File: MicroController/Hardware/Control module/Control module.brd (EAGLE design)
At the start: 100 x 60 mm, 54 parts, among them J1 1X2-3.5MM, J2 RJ45-TRAFO, J3 RJ45-TRAFO, J4 RJ45-TRAFO, Q1 BSS138, Q2 BSS138, Q3 BSS138, Q4 BSS138, Q5 BSS138, Q6 BSS138, Q7 BSS138, Q8 BSS138, U1 CD74HC4067SM96, U3 TLV1117-33CDCY

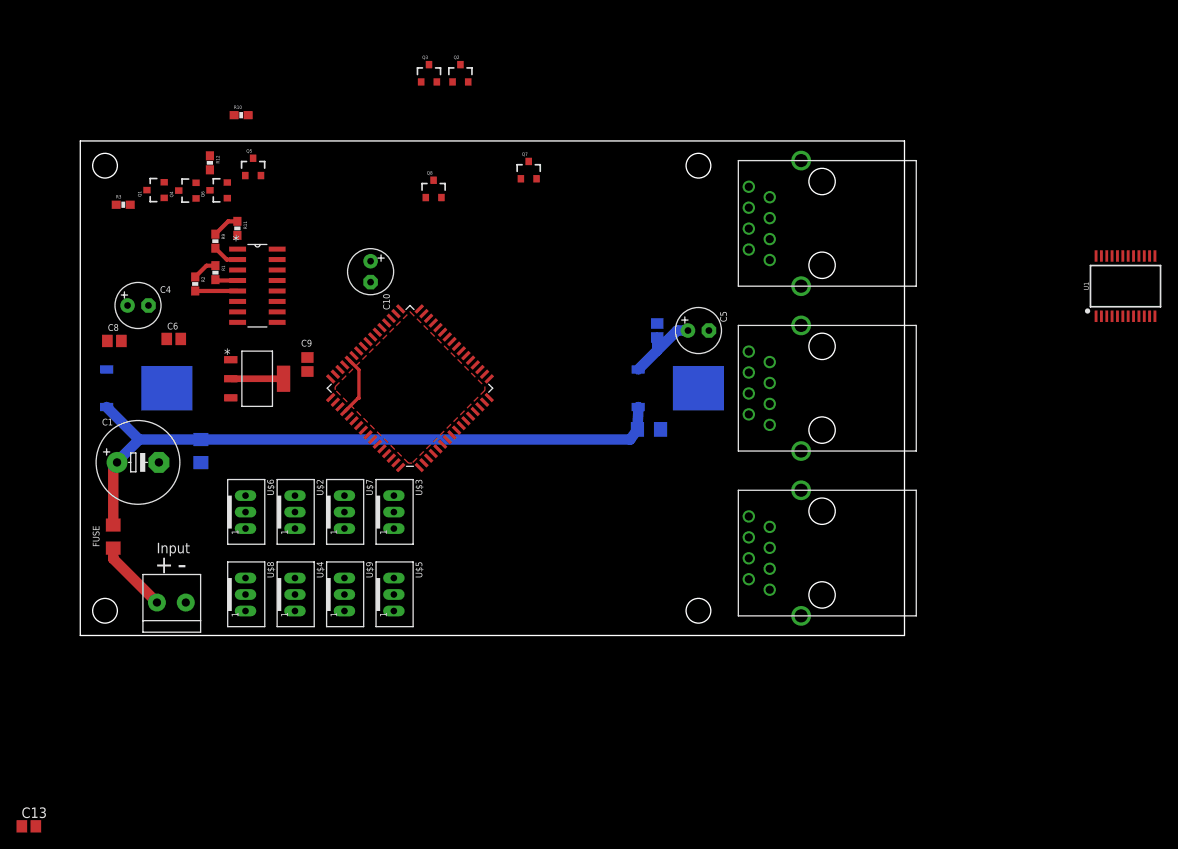
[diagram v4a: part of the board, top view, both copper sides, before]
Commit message: Connected several components, added RX TX connector
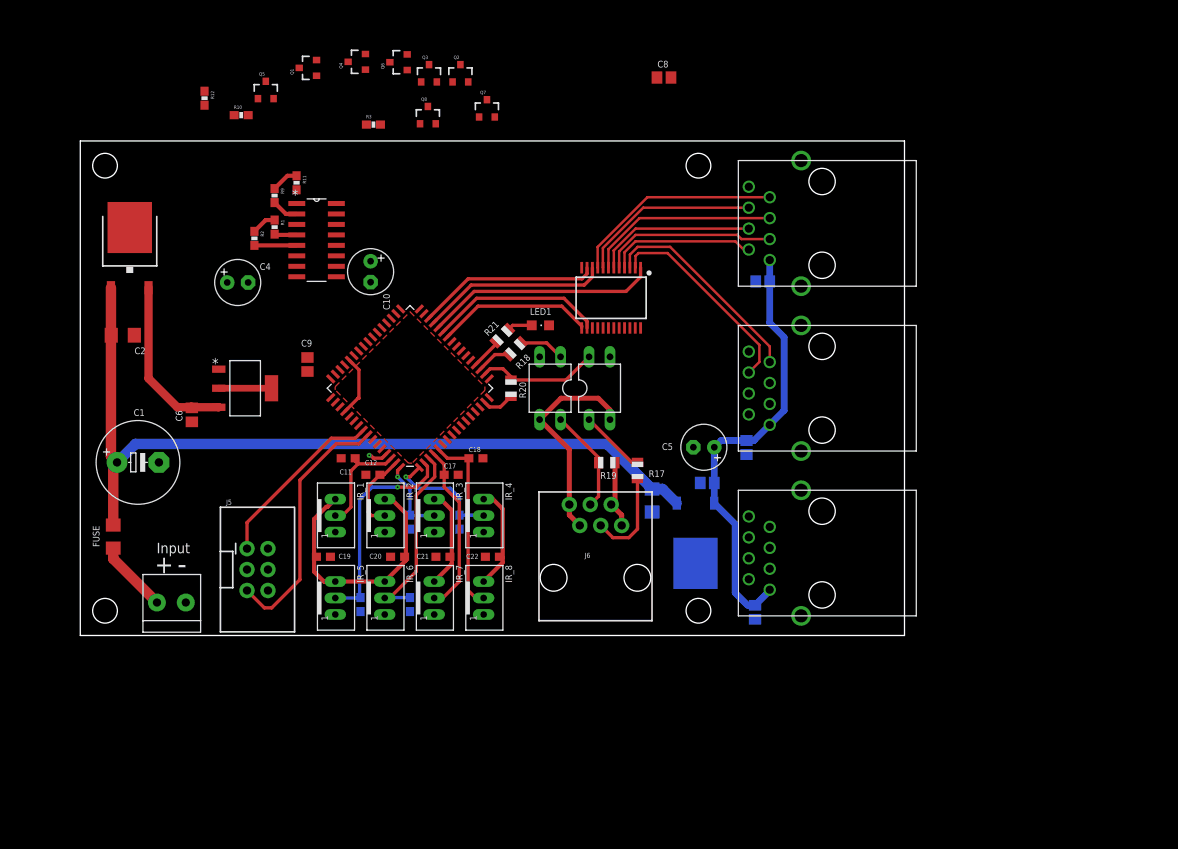
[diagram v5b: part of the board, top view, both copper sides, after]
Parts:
- removed U$2, U$3, U$4, U$5, U$6, U$7, U$8, U$9: JST-PH_3-PIN_HEADER, SRG:JST_B3B-PH_HEADER
- added C11, C12, C14, C15, C16, C17, C18, C19, C20, C21, C22: (no value), adafruit:C0603
- added C23, C24, C25: (no value), adafruit:C0805
- added IR_1, IR_2, IR_3, IR_4, IR_5, IR_6, IR_7, IR_8: JST-PH_3-PIN_HEADER, SRG:JST_B3B-PH_HEADER
- added J5: (no value), SparkFun-Connectors:2X3-SHROUDED
- added J6: RJ11, SparkFun-Connectors:RJ11-6
- added LED1: (no value), led:CHIPLED_0805
- added OC1, OC2: (no value), optocoupler:DIL04
- added R17, R18, R19, R20, R21: 10K, adafruit:R0805
- C13: device adafruit:C0805 -> adafruit:C0603
- moved C8 73.9 mm to (70.8, 67.7)
- moved U1 62.4 mm to (64.4, 41.0), turned to 180 degrees
- moved C13 48.4 mm to (34.0, 3.75), flipped to the bottom, turned to 270 degrees
- moved R3 31.9 mm to (35.6, 62.0)
- moved Q6 26.8 mm to (38.7, 69.6)
- moved Q4 25.8 mm to (33.6, 69.6)
- moved Q1 23.7 mm to (27.7, 68.9)
- moved C7 19.5 mm to (76.1, 18.5), turned to 0 degrees
- moved 5V_REGULATOR 18.9 mm to (74.6, 11.3), turned to 180 degrees
- moved 12V_REGULATOR 17.1 mm to (6.00, 47.0), flipped to the top, turned to 0 degrees
- moved C2 16.9 mm to (5.16, 36.4), flipped to the top, turned to 0 degrees
- moved C5 14.2 mm to (75.7, 22.8), turned to 180 degrees
- moved C4 12.4 mm to (19.1, 42.8)
- moved C6 9.47 mm to (13.5, 26.8), turned to 270 degrees
- moved Q5 9.46 mm to (22.5, 66.1)
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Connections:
- new net GND_RASPI: J6.1, J6.2, OC1.3, OC2.2
- new net N$1: OC1.1, R18.1
- new net N$2: OC2.1, R17.1
- new net N$3: R21.2, U$1.20
- new net N$4: LED1.A, R21.1
- new net PDI_DATA: J5.1, U$1.56
- new net RESET_PDI_CLK: J5.5, U$1.57
- new net RX_ATXMEGA: OC2.4, R20.1, U$1.18
- new net RX_RASPI: J6.3, OC1.4, R19.1
- new net S0: U$1.29, U1.10
- new net S1: U$1.30, U1.11
- new net S2: U$1.27, U1.14
- new net S3: U$1.26, U1.13
- new net TX_ATXMEGA: R18.2, U$1.19
- new net TX_RASPI: J6.4, R17.2
- new net ULTRA1: J2.7, U1.9
- new net ULTRA2: J2.6, U1.8
- new net ULTRA_COM: U$1.28, U1.1
- new net VCC_RASPI: J6.5, J6.6, R19.2
- net +5V: now also C23.1, C24.1, C25.1, J2.1, J3.1, J4.1
- net GND: now also C11.2, C12.2, C13.2, C14.2, C15.2, C16.2, C17.2, C18.2, C19.2, C20.2, C21.2, C22.2, C23.2, C24.2, C25.2, IR_1.P1, IR_2.P1, IR_3.P1, IR_4.P1, IR_5.P1, IR_6.P1, IR_7.P1, IR_8.P1, J5.6, LED1.C, OC1.2, OC2.3; no longer U$2.P3, U$3.P3, U$4.P3, U$5.P3, U$6.P3, U$7.P3, U$8.P3, U$9.P3
- net IR_1: now also C11.1, IR_1.P2, U$1.62; no longer U$6.P2
- net IR_2: now also C12.1, IR_2.P2, U$1.63; no longer U$2.P2
- net IR_3: now also C14.1, IR_3.P2, U$1.64; no longer U$7.P2
- net IR_4: now also C15.1, IR_4.P2, U$1.1; no longer U$3.P2
- net IR_5: now also C13.1, IR_5.P2, U$1.2; no longer U$8.P2
- net IR_6: now also C16.1, IR_6.P2, U$1.3; no longer U$4.P2
- net IR_7: now also C17.1, IR_7.P2, U$1.4; no longer U$9.P2
- net IR_8: now also C18.1, IR_8.P2, U$1.5; no longer U$5.P2
- net ULTRA13: now also J3.2
- net ULTRA14: now also J3.3
- net ULTRA15: now also J3.4
- net ULTRA16: now also J3.5
- net ULTRA3: now also J2.5
- net ULTRA4: now also J2.4
- net ULTRA5: now also J2.3
- net ULTRA6: now also J2.2
- net ULTRA7: now also J3.7
- net ULTRA8: now also J3.6
- net VCC: now also C19.1, C20.1, C21.1, C22.1, IR_1.P3, IR_2.P3, IR_3.P3, IR_4.P3, IR_5.P3, IR_6.P3, IR_7.P3, IR_8.P3, J5.2, R20.2; no longer U$2.P1, U$3.P1, U$4.P1, U$5.P1, U$6.P1, U$7.P1, U$8.P1, U$9.P1
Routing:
- net VCC: track 12.7 -> 76.8 mm, vias 0 -> 1
- net +5V: track 9.56 -> 53.7 mm
- net RESET_PDI_CLK: track 0.00 -> 31.3 mm
- net ULTRA_COM: track 0.00 -> 28.2 mm
- net IR_5: track 0.00 -> 26.2 mm, vias 0 -> 1
- net GND_RASPI: track 0.00 -> 26.2 mm
- net ULTRA1: track 0.00 -> 25.9 mm
- net ULTRA7: track 0.00 -> 25.8 mm
- net ULTRA8: track 0.00 -> 25.1 mm
- net ULTRA3: track 0.00 -> 23.4 mm
- net IR_6: track 0.00 -> 23.2 mm
- net S0: track 0.00 -> 22.7 mm
- net IR_8: track 0.00 -> 22.6 mm
- net S1: track 0.00 -> 22.2 mm
- net ULTRA2: track 0.00 -> 22.1 mm
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
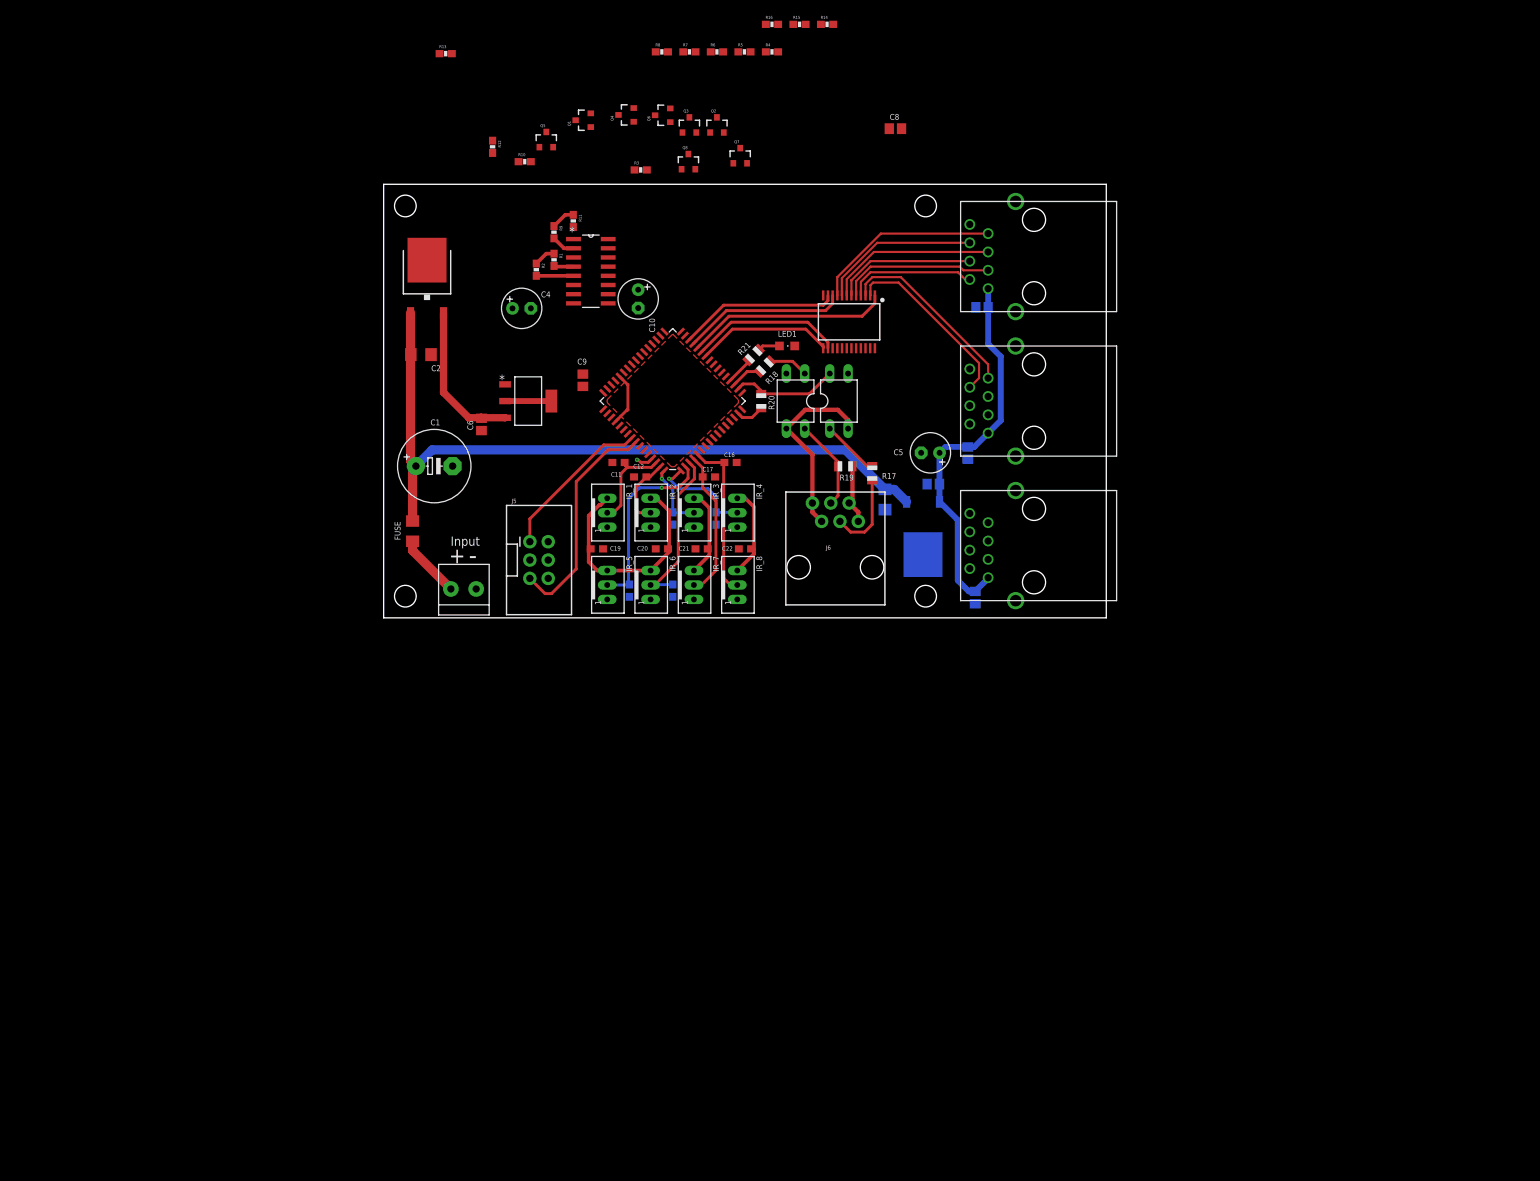
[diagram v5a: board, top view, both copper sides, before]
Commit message: Changed many things in the layout.
Added more I/O and connectivity to the Raspberry Pi.
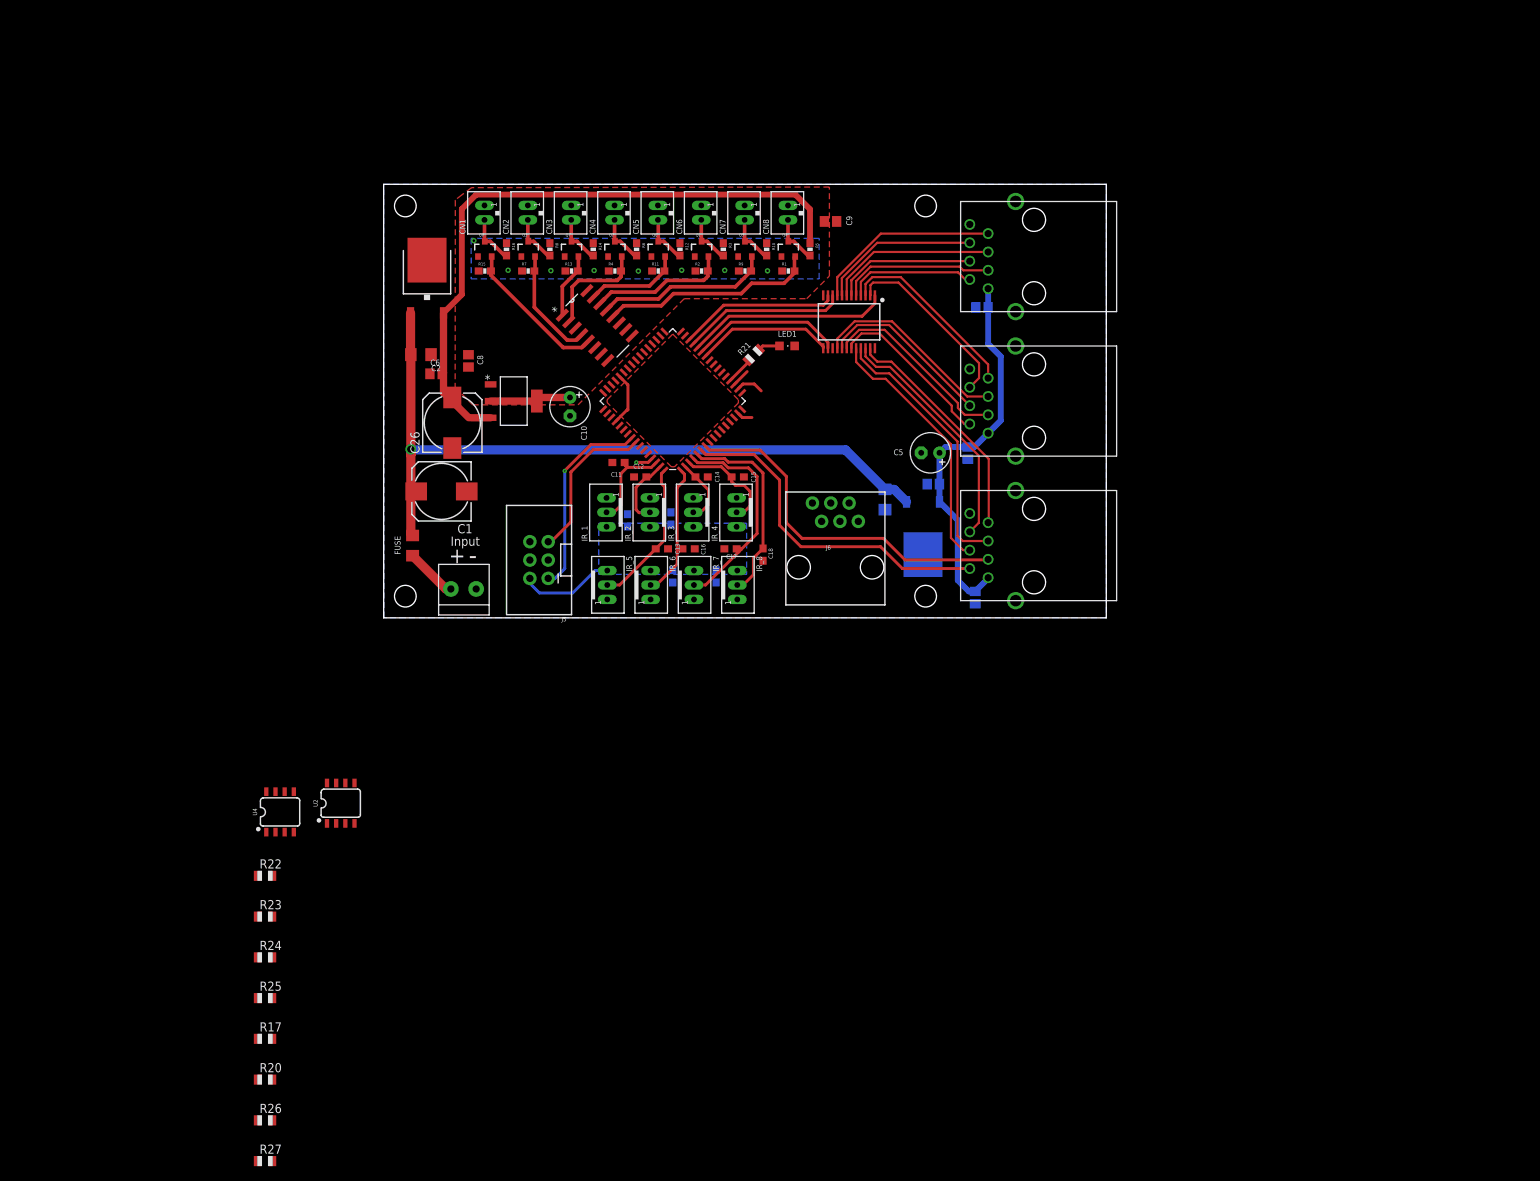
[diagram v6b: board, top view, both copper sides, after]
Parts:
- removed C4: (no value), adafruit:E2,5-6
- removed OC1, OC2: (no value), optocoupler:DIL04
- removed R18, R19: 10K, adafruit:R0805
- added C26: (no value), adafruit:175TMP-0810
- added CN1, CN2, CN3, CN4, CN5, CN6, CN7, CN8: JST-PH_2-PIN_HEADER, SRG:JST_B2B-PH_HEADER
- added R22, R23, R24, R25, R26, R27: 10K, adafruit:R0805
- added U2, U4: DUAL-OPTOISOLATOR_SOIC8, SparkFun-DiscreteSemi:SO08
- C1: device adafruit:E5-10,5 -> adafruit:175TMP-0810
- moved R20 116.3 mm to (-16.4, -63.9), turned to 0 degrees
- moved R17 114.8 mm to (-16.4, -58.3), turned to 0 degrees
- moved C8 67.3 mm to (11.7, 35.6), turned to 270 degrees
- moved R15 55.3 mm to (14.0, 48.0)
- moved R16 48.2 mm to (17.0, 51.0), turned to 270 degrees
- moved R14 44.9 mm to (29.0, 51.0), turned to 270 degrees
- moved C9 40.7 mm to (61.8, 54.9), turned to 0 degrees
- moved R7 37.6 mm to (20.0, 48.0)
- moved R4 37.3 mm to (32.0, 48.0)
- moved R10 35.6 mm to (53.0, 51.0), turned to 270 degrees
- moved R13 34.8 mm to (26.0, 48.0)
- moved R1 32.5 mm to (56.0, 48.0), turned to 0 degrees
- moved R8 31.4 mm to (23.0, 51.0), turned to 270 degrees
- moved Q5 31.4 mm to (50.0, 51.0)
- moved Q8 30.7 mm to (14.0, 51.0)
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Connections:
- removed net N$1: OC1.1, R18.1
- new net N$5: R23.1, U2.3
- new net N$6: R22.1, U2.1
- new net N$8: R20.1, U4.3
- new net RES_RASPI: J6.1, R23.2
- new net SIGNAL_ATXMEGA: R17.2
- new net SIGNAL_RASPI: J6.5, R26.1, U4.8
- new net TRIGGER_1: J4.2, U$1.6
- new net TRIGGER_2: J4.3, U$1.7
- net +12V: now also C26.+; no longer C4.+
- net GND: now also C26.-, CN1.P1, CN2.P1, CN3.P1, CN4.P1, CN5.P1, CN6.P1, CN7.P1, CN8.P1, U2.5, U2.7, U4.2, U4.4; no longer C4.-, OC1.2, OC2.3
- net GND_RASPI: now also U2.2, U2.4, U4.5, U4.7; no longer J6.1, OC1.3, OC2.2
- net IR_3: now also U$1.2; no longer U$1.64
- net IR_4: now also U$1.3; no longer U$1.1
- net IR_5: now also U$1.64; no longer U$1.2
- net IR_6: now also U$1.1; no longer U$1.3
- net MOTOR_1: now also CN1.P2
- net MOTOR_2: now also CN2.P2
- net MOTOR_3: now also CN3.P2
- net MOTOR_4: now also CN4.P2
- net MOTOR_5: now also CN5.P2
- net MOTOR_6: now also CN6.P2
- net MOTOR_7: now also CN7.P2
- net MOTOR_8: now also CN8.P2
- net MOTOR_LEVEL_1: now also MOTOR_CONTROL_DEMULTIPLEXER.5; no longer MOTOR_CONTROL_DEMULTIPLEXER.13
- net MOTOR_LEVEL_2: now also MOTOR_CONTROL_DEMULTIPLEXER.4; no longer MOTOR_CONTROL_DEMULTIPLEXER.14
- net MOTOR_LEVEL_3: now also MOTOR_CONTROL_DEMULTIPLEXER.1; no longer MOTOR_CONTROL_DEMULTIPLEXER.15
- net MOTOR_LEVEL_4: now also MOTOR_CONTROL_DEMULTIPLEXER.2; no longer MOTOR_CONTROL_DEMULTIPLEXER.12
- net MOTOR_LEVEL_5: now also MOTOR_CONTROL_DEMULTIPLEXER.15; no longer MOTOR_CONTROL_DEMULTIPLEXER.1
- net MOTOR_LEVEL_6: now also MOTOR_CONTROL_DEMULTIPLEXER.14; no longer MOTOR_CONTROL_DEMULTIPLEXER.5
- net MOTOR_LEVEL_7: now also MOTOR_CONTROL_DEMULTIPLEXER.13; no longer MOTOR_CONTROL_DEMULTIPLEXER.2
- net MOTOR_LEVEL_8: now also MOTOR_CONTROL_DEMULTIPLEXER.12; no longer MOTOR_CONTROL_DEMULTIPLEXER.4
- net N$2: now also U4.1; no longer OC2.1
- net RESET_PDI_CLK: now also R24.1, U2.6
- net RX_ATXMEGA: now also R25.1, U2.8; no longer OC2.4, R20.1
- net RX_RASPI: now also R27.1, U4.6; no longer OC1.4, R19.1
- net TX_ATXMEGA: now also R20.2; no longer R18.2
- net TX_RASPI: now also R22.2; no longer R17.2
- net ULTRA10: now also J4.6
- net ULTRA11: now also J4.5
- net ULTRA12: now also J4.4
- net ULTRA9: now also J4.7
- net VCC: now also R24.2, R25.2, R26.2, R27.2; no longer R20.2
- net VCC_RASPI: no longer J6.5, R19.2
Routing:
- net +12V: track 21.2 -> 89.7 mm
- net TRIGGER_2: track 0.00 -> 49.4 mm
- net VCC: track 76.8 -> 29.0 mm, vias 1 -> 9
- net TRIGGER_1: track 0.00 -> 47.6 mm
- net ULTRA11: track 0.00 -> 37.1 mm
- net ULTRA12: track 0.00 -> 36.0 mm
- net ULTRA10: track 0.00 -> 33.6 mm
- net ULTRA9: track 0.00 -> 32.1 mm
- net ULTRA16: track 0.00 -> 27.5 mm
- net MOTOR_LEVEL_8: track 2.79 -> 29.9 mm
- net ULTRA14: track 0.00 -> 26.4 mm
- net GND_RASPI: track 26.2 -> 0.00 mm
- net ULTRA15: track 0.00 -> 24.3 mm
- net ULTRA13: track 0.00 -> 23.2 mm
- net MOTOR_LEVEL_7: track 3.27 -> 24.3 mm
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- added copper zone on layer 16, net GND
- added copper zone on layer 1, net VCC
- added copper zone on layer 16, net VCC
